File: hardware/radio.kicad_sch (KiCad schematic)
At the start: 44 parts, among them J101 Cortex_Debug, J102 JAE_DX07S016JA3, SW101 SW_Push, SW102 SW_Push, U101 TPS78433QWDRBRQ1, U102 ATSAMD51G, U103 E62, Y101 32k768

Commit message: Refresh
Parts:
- D101, D102: LCSC (none) -> C965555; Manufacturer (none) -> Worldsemi; Product (none) -> WS2812B-2020
- ESD101: Manufacturer (none) -> Semtech; Mouser (none) -> 947-RCLAMP0582N.TCT; Product (none) -> RCLAMP0582N.TCT
- J102: Manufacturer (none) -> JAE Electronics; Mouser (none) -> 656-DX07S016JA3R1500; Product (none) -> DX07S016JA3R1500
- TVS101: Manufacturer (none) -> Bourns; Mouser (none) -> 652-CG0603MLC-05LE; Product (none) -> CG0603MLC-05LE; Rating (none) -> 5V
- U101: Manufacturer (none) -> Texas Instruments; Mouser (none) -> 595-TPS78433QWDRBRQ1; Product (none) -> TPS78433QWDRBRQ1
- U102: Manufacturer (none) -> Microchip Technology; Mouser (none) -> 556-ATSAMD51G19AMU; Product (none) -> ATSAMD51G19A-MU
- renumbered C103 to C102, C104 to C103, C105 to C104, C106 to C105, C107 to C106, C108 to C107, C109 to C108, C110 to C109, C111 to C110, C303 to C111

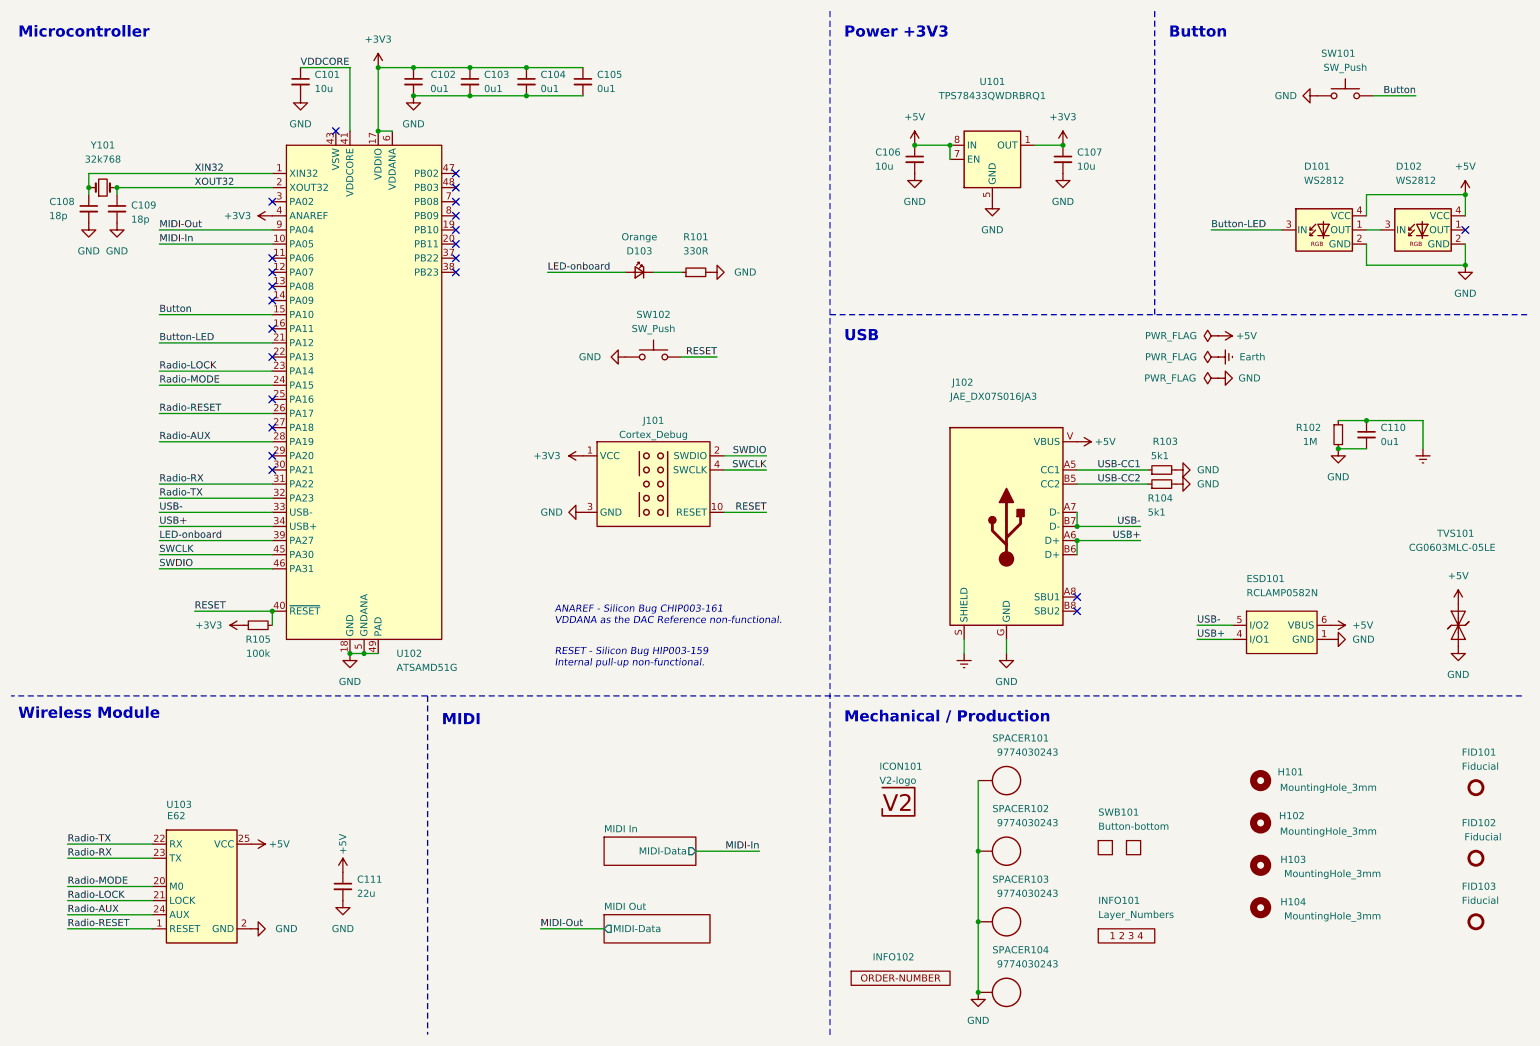
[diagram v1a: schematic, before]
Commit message: Replace Order_Number
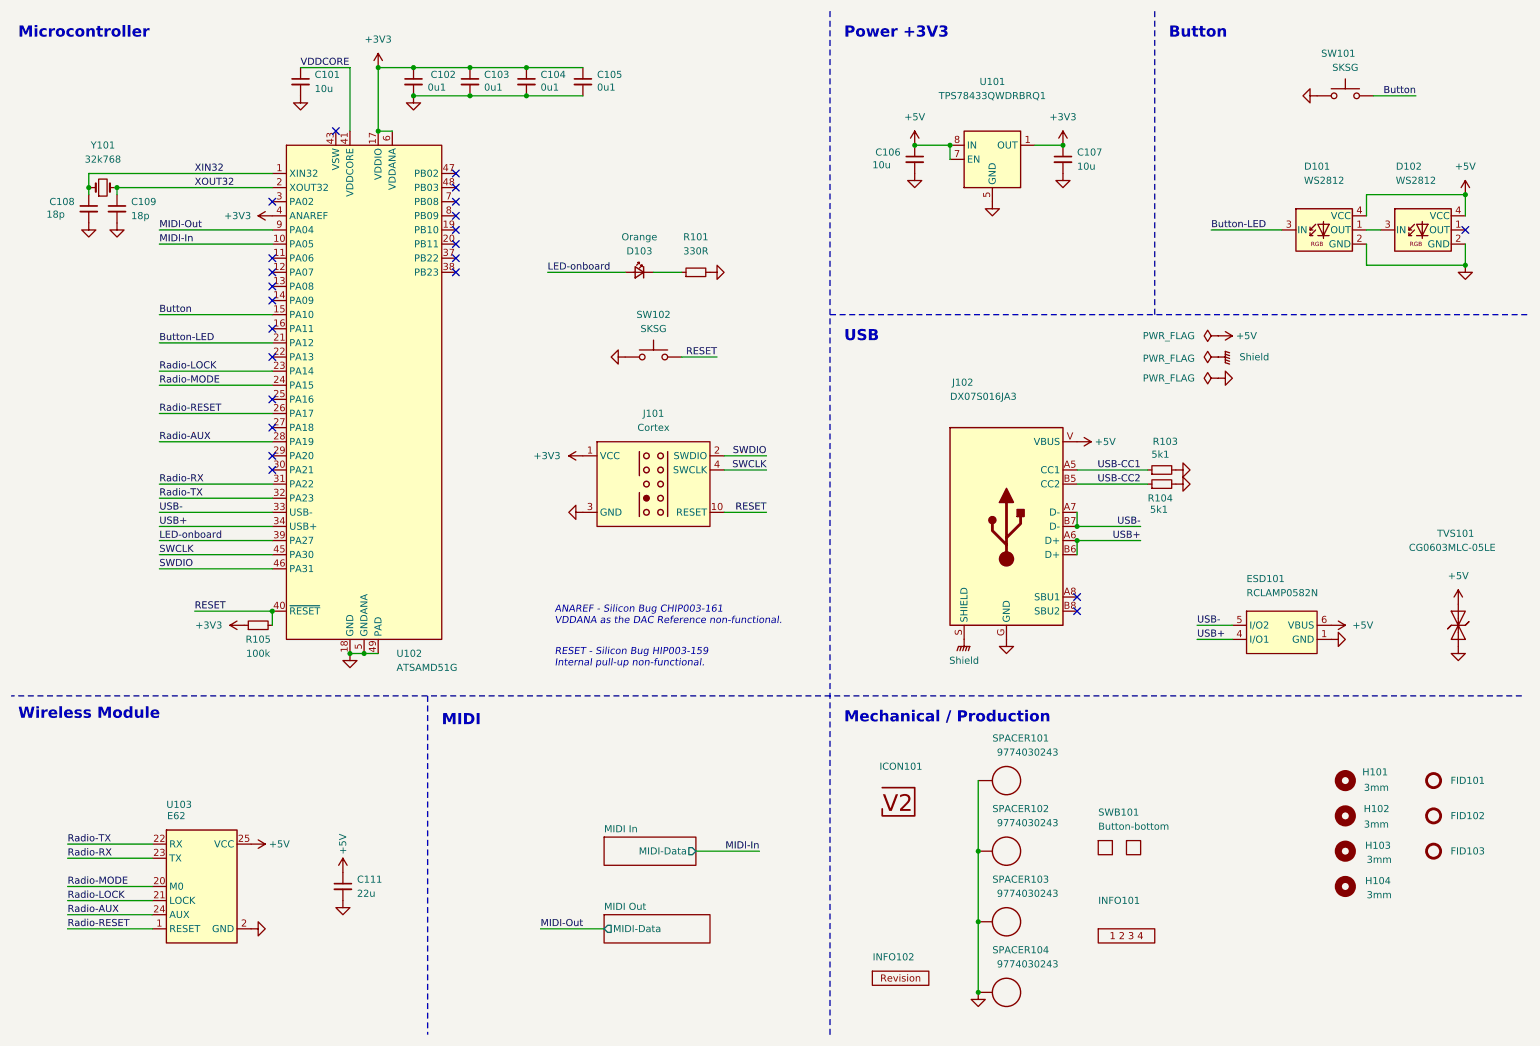
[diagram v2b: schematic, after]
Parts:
- removed C110: 0u1, Capacitor_SMD:C_0603_1608Metric, symbol Device:C_Small
- removed R102: 1M, Resistor_SMD:R_0603_1608Metric, symbol Device:R_Small
- C101: footprint Capacitor_SMD:C_0603_1608Metric -> V2_Capacitor_SMD:C_0603; symbol Device:C_Small -> V2_Device:C_0603_10u; Manufacturer (none) -> TDK; Mouser (none) -> 810-C1608X6S1A106M; Product (none) -> C1608X6S1A106M080AC; Rating (none) -> 10V
- C102, C103, C104, C105: footprint Capacitor_SMD:C_0603_1608Metric -> V2_Capacitor_SMD:C_0603; symbol Device:C_Small -> V2_Device:C_0603_0u1; Manufacturer (none) -> TDK; Mouser (none) -> 810-CGA3E2X7R1H104MA; Product (none) -> CGA3E2X7R1H104M080AA; Rating (none) -> 50V
- C106, C107: footprint Capacitor_SMD:C_0603_1608Metric -> V2_Capacitor_SMD:C_0805; symbol Device:C_Small -> V2_Device:C_0805_10u; Manufacturer (none) -> TDK; Mouser (none) -> 810-C2012X5R1E106K; Product (none) -> C2012X5R1E106K125AB; Rating (none) -> 25V
- C108, C109: footprint Capacitor_SMD:C_0603_1608Metric -> V2_Capacitor_SMD:C_0603; symbol Device:C_Small -> V2_Device:C_0603_18p; Manufacturer (none) -> YAGEO; Mouser (none) -> 603-CC603JRNPO9BN180; Product (none) -> CC0603JRNPO9BN180
- C111: footprint Capacitor_SMD:C_1210_3225Metric -> V2_Capacitor_SMD:C_1210; symbol Device:C_Small -> V2_Device:C_1210_22u; Manufacturer (none) -> TDK; Mouser (none) -> 810-CGA6P3X7R1E226M5; Product (none) -> CGA6P3X7R1E226M250AE; Rating (none) -> 25V
- D103: footprint LED_SMD:LED_0603_1608Metric -> V2_LED:LED_0603; symbol Device:LED_Small -> V2_Device:LED_0603_Orange; Manufacturer (none) -> ROHM Semiconductor; Mouser (none) -> 755-SML-D12D1WT86; Product (none) -> SML-D12D1WT86
- FID101, FID102, FID103: value Fiducial -> Fiducial_Paste
- H101, H102, H103, H104: value MountingHole_3mm -> 3mm
- INFO102: value ORDER-NUMBER -> ~; footprint V2_Production:Order_Number -> V2_Production:Revision; symbol V2_Production:Order_Number -> V2_Production:Revision
- J101: value Cortex_Debug -> Cortex; footprint V2_Cortex_Debug:Cortex_Debug_Pad -> V2_Connector_Debug:Cortex; symbol V2_Cortex_Debug:Cortex_Debug -> V2_Connector_Debug:Cortex
- J102: value JAE_DX07S016JA3 -> DX07S016JA3
- R101: footprint Resistor_SMD:R_0603_1608Metric -> V2_Resistor_SMD:R_0603; symbol Device:R_Small -> V2_Device:R_0603_330R; Manufacturer (none) -> Vishay; Mouser (none) -> 71-CRCW0603330RFKEAC; Product (none) -> CRCW0603330RFKEAC; Rating (none) -> 100mW
- R103, R104: footprint Resistor_SMD:R_0603_1608Metric -> V2_Resistor_SMD:R_0603; symbol Device:R_Small -> V2_Device:R_0603_5k1; Manufacturer (none) -> Vishay; Mouser (none) -> 71-CRCW06035K10FKEAC; Product (none) -> CRCW06035K10FKEAC; Rating (none) -> 100mW
- R105: footprint Resistor_SMD:R_0603_1608Metric -> V2_Resistor_SMD:R_0603; symbol Device:R_Small -> V2_Device:R_0603_100k; Manufacturer (none) -> Vishay; Mouser (none) -> 71-CRCW0603100KFKEAC; Product (none) -> CRCW0603100KFKEAC; Rating (none) -> 100mW
- SW101, SW102: value SW_Push -> SKSG; symbol Switch:SW_Push -> V2_Switch:SKSG; Manufacturer (none) -> Alps Alpine; Mouser (none) -> 688-SKSGACE010; Product (none) -> SKSGACE010
- TVS101: footprint Diode_SMD:D_0603_1608Metric -> V2_Diode_SMD:D_0603
- Y101: symbol Device:Crystal_Small -> V2_Device:Crystal_3.2x1.5_32k768; Manufacturer (none) -> ABRACON; Mouser (none) -> 815-ABS0716632.768KT; Product (none) -> ABS07-166-32.768KHZ-T
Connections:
- net Earth renamed Shield
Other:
- moved on the sheet: FID101, FID102, FID103, H101, H102, H103, H104

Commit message: Update Library
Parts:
- C101: symbol V2_Device:C_0603_10u -> V2_Capacitor:0603_10u
- C102, C103, C104, C105: symbol V2_Device:C_0603_0u1 -> V2_Capacitor:0603_0u1
- C106, C107: symbol V2_Device:C_0805_10u -> V2_Capacitor:0805_10u
- C108, C109: symbol V2_Device:C_0603_18p -> V2_Capacitor:0603_18p
- C111: value 22u -> 10u; symbol V2_Device:C_1210_22u -> V2_Capacitor:1210_22u
- D103: symbol V2_Device:LED_0603_Orange -> V2_LED:0603_Orange
- R101: symbol V2_Device:R_0603_330R -> V2_Resistor:0603_330R
- R103, R104: symbol V2_Device:R_0603_5k1 -> V2_Resistor:0603_5k1
- R105: symbol V2_Device:R_0603_100k -> V2_Resistor:0603_100k
- Y101: symbol V2_Device:Crystal_3.2x1.5_32k768 -> V2_Crystal:3.2x1.5_32k768

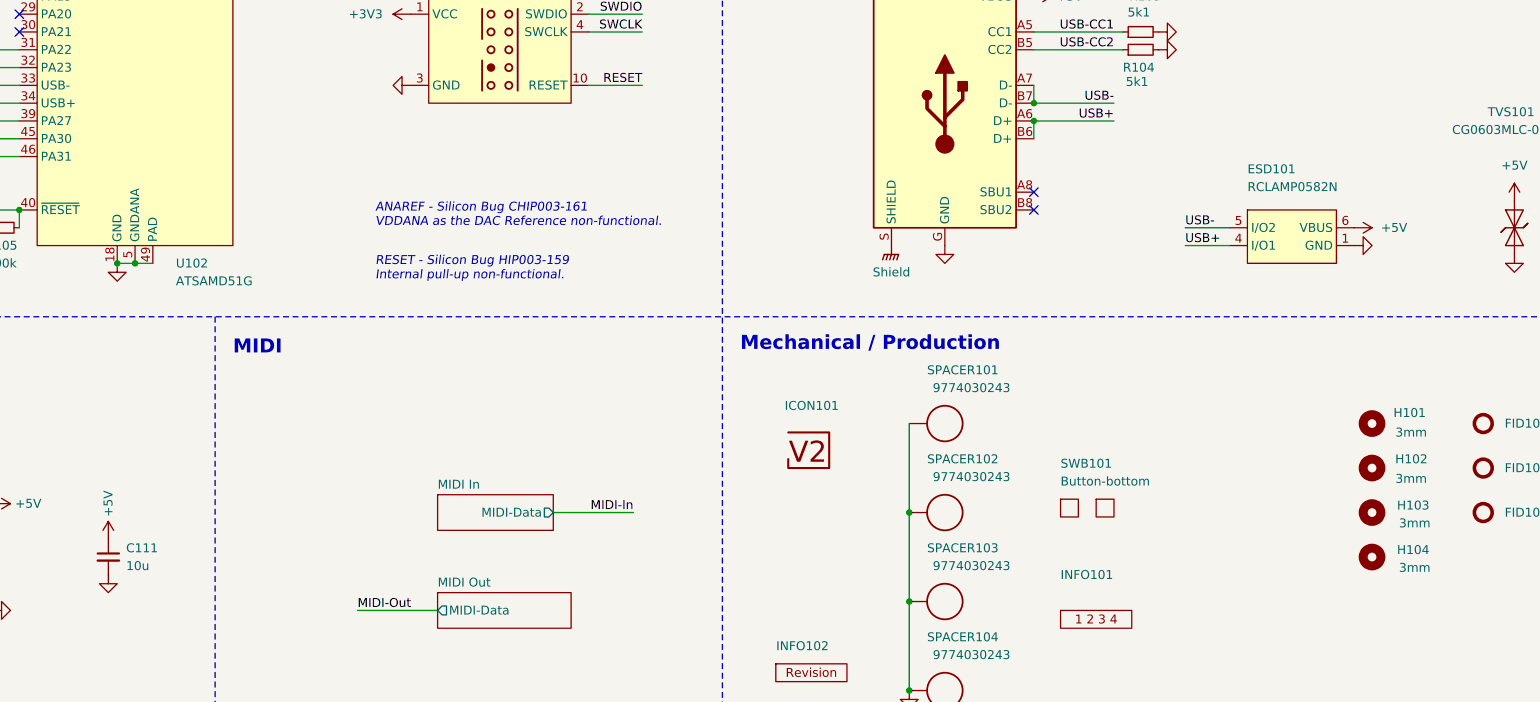
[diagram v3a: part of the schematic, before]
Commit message: Update ESD suppressor
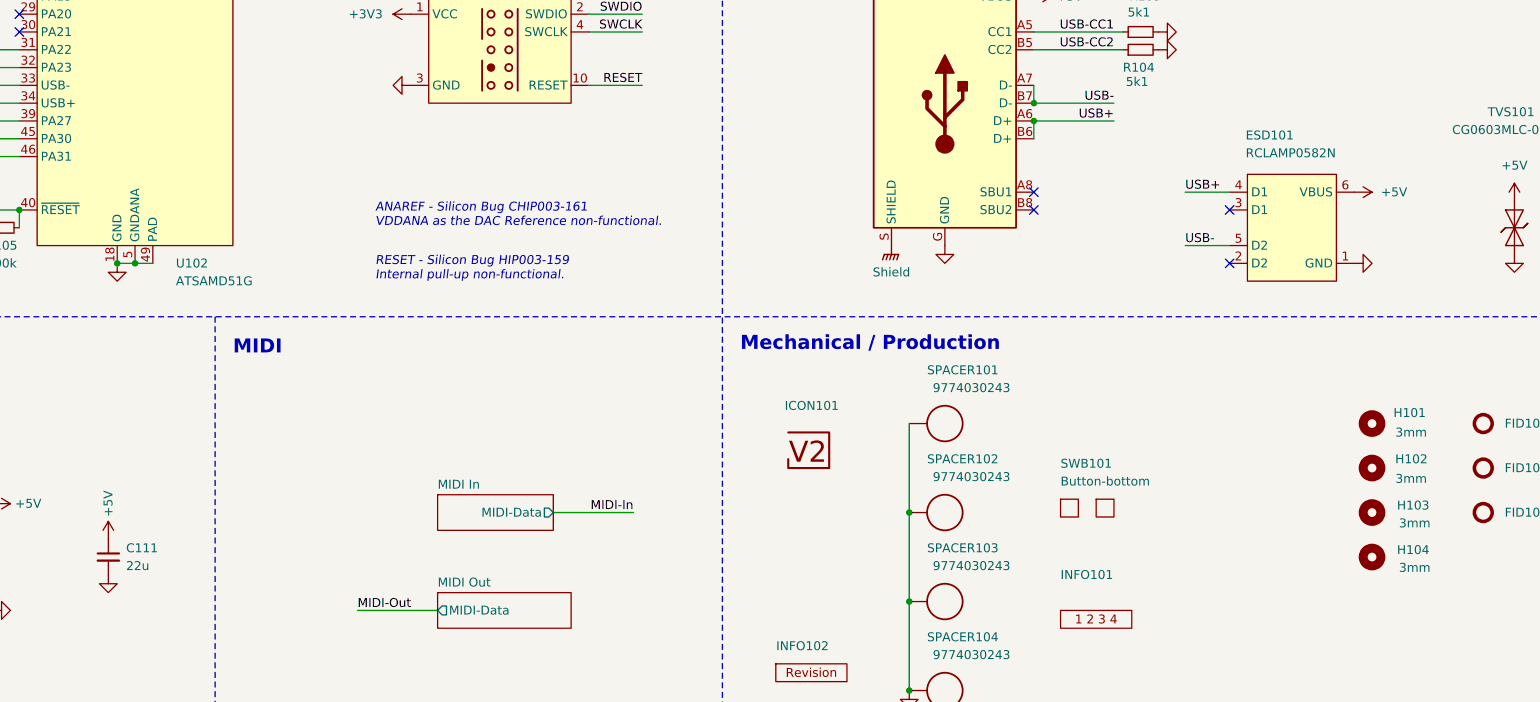
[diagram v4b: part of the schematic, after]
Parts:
- C108, C109: Manufacturer YAGEO -> TDK; Mouser 603-CC603JRNPO9BN180 -> 810-CGA3E2C0G1H180J; Product CC0603JRNPO9BN180 -> CGA3E2C0G1H180J080AA
- C111: value 10u -> 22u
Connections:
- no-connect marks 23 -> 25
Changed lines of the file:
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@@
 	(title_block
 		(title "V2 radio")
-		(date "2026-02-10")
+		(date "2026-03-14")
 		(rev "2026-02-10")
 		(company "Versio Duo")
@@
 	)
 	(no_connect
+		(at 232.41 120.65)
+	)
+	(no_connect
+		(at 232.41 128.27)
+	)
+	(no_connect
 		(at 71.12 34.29)
 	)
@@
 	(wire
 		(pts
-			(xy 226.06 123.19) (xy 232.41 123.19)
+			(xy 226.06 125.73) (xy 232.41 125.73)
 		)
 		(stroke
@@
 	(wire
 		(pts
+			(xy 226.06 118.11) (xy 232.41 118.11)
+		)
+		(stroke
+			(width 0)
+			(type default)
+		)
+	)
+	(wire
+		(pts
 			(xy 95.25 27.94) (xy 105.41 27.94)
 		)
@@
 	(wire
 		(pts
-			(xy 226.06 125.73) (xy 232.41 125.73)
-		)
-		(stroke
-			(width 0)
-			(type default)
-		)
-	)
-	(wire
-		(pts
 			(xy 109.22 59.69) (xy 123.19 59.69)
 		)
@@
 		)
 	)
-	(label "SWCLK"
-		(at 39.37 110.49 0)
+	(label "USB+"
+		(at 226.06 118.11 0)
 		(effects
 			(font
@@
 		)
 	)
-	(label "SWDIO"
-		(at 39.37 113.03 0)
+	(label "SWCLK"
+		(at 39.37 110.49 0)
 		(effects
 			(font
@@
 		)
 	)
-	(label "Button"
-		(at 39.37 67.31 0)
+	(label "SWDIO"
+		(at 39.37 113.03 0)
 		(effects
 			(font
@@
 		)
 	)
-	(label "USB+"
-		(at 226.06 125.73 0)
+	(label "Button"
+		(at 39.37 67.31 0)
 		(effects
 			(font
@@
 	)
 	(label "USB-"
-		(at 226.06 123.19 0)
+		(at 226.06 125.73 0)
 		(effects
 			(font
@@
 			)
 		)
-		(property "Description" "Unpolarized capacitor, small symbol"
+		(property "Description" ""
 			(at 115.57 38.1 0)
 			(effects
@@
 		(dnp no)
 		(property "Reference" "ESD101"
-			(at 234.95 115.57 0)
+			(at 234.696 110.744 0)
 			(effects
 				(font
@@
 		)
 		(property "Value" "RCLAMP0582N"
-			(at 234.95 118.11 0)
+			(at 234.696 113.284 0)
 			(effects
 				(font
@@
 			)
 		)
-		(property "Description" "Push button switch, generic, two pins"
+		(property "Description" "Push button"
 			(at 252.73 27.94 0)
 			(effects
@@
 	(symbol
 		(lib_id "V2_power:+5V")
-		(at 250.19 123.19 270)
+		(at 250.19 118.11 270)
 		(unit 1)
 		(exclude_from_sim no)
@@
 		(dnp no)
 		(property "Reference" "#PWR129"
-			(at 246.38 123.19 0)
+			(at 246.38 118.11 0)
 			(effects
 				(font
@@
 		)
 		(property "Value" "+5V"
-			(at 254 123.19 90)
+			(at 254 118.11 90)
 			(effects
 				(font
@@
 		)
 		(property "Footprint" ""
-			(at 250.19 123.19 0)
+			(at 250.19 118.11 0)
 			(effects
 				(font
@@
 		)
 		(property "Datasheet" ""
-			(at 250.19 123.19 0)
+			(at 250.19 118.11 0)
 			(effects
 				(font
@@
 		)
 		(property "Description" ""
-			(at 250.19 123.19 0)
+			(at 250.19 118.11 0)
 			(effects
 				(font
@@
 			)
 		)
-		(property "Description" "Light emitting diode, small symbol"
+		(property "Description" ""
 			(at 125.73 59.69 0)
 			(effects
@@
 			)
 		)
-		(property "Description" "Unpolarized capacitor, small symbol"
+		(property "Description" ""
 			(at 201.93 52.07 0)
 			(effects
@@
 			)
 		)
-		(property "Description" "Resistor, small symbol"
+		(property "Description" ""
 			(at 232.41 97.79 0)
 			(effects
@@
 			)
 		)
-		(property "Value" "10u"
+		(property "Value" "22u"
 			(at 74.93 171.45 0)
 			(effects
@@
 			)
 		)
-		(property "Description" "Unpolarized capacitor, small symbol"
+		(property "Description" ""
 			(at 72.39 182.88 0)
 			(effects
@@
 			)
 		)
-		(property "Description" "Unpolarized capacitor, small symbol"
+		(property "Description" ""
 			(at 175.26 52.07 0)
 			(effects
@@
 			)
 		)
-		(property "Description" "Two pin crystal, small symbol"
+		(property "Description" ""
 			(at 29.21 44.45 0)
 			(effects
@@
 			)
 		)
-		(property "Description" "Unpolarized capacitor, small symbol"
+		(property "Description" ""
 			(at 31.75 62.738 0)
 			(effects
@@
 			)
 		)
-		(property "Mouser" "603-CC603JRNPO9BN180"
+		(property "Mouser" "810-CGA3E2C0G1H180J"
 			(at 31.75 71.628 0)
 			(effects
@@
 			)
 		)
-		(property "Product" "CC0603JRNPO9BN180"
+		(property "Product" "CGA3E2C0G1H180J080AA"
 			(at 31.75 68.834 0)
 			(effects
@@
 			)
 		)
-		(property "Manufacturer" "YAGEO"
+		(property "Manufacturer" "TDK"
 			(at 31.75 66.04 0)
 			(effects
@@
 			)
 		)
-		(property "Description" "Unpolarized capacitor, small symbol"
+		(property "Description" ""
 			(at 64.77 40.64 0)
 			(effects
@@
 			)
 		)
-		(property "Description" "Unpolarized capacitor, small symbol"
+		(property "Description" ""
 			(at 26.67 62.738 0)
 			(effects
@@
 			)
 		)
-		(property "Mouser" "603-CC603JRNPO9BN180"
+		(property "Mouser" "810-CGA3E2C0G1H180J"
 			(at 26.67 71.628 0)
 			(effects
@@
 			)
 		)
-		(property "Product" "CC0603JRNPO9BN180"
+		(property "Product" "CGA3E2C0G1H180J080AA"
 			(at 26.67 68.834 0)
 			(effects
@@
 			)
 		)
-		(property "Manufacturer" "YAGEO"
+		(property "Manufacturer" "TDK"
 			(at 26.67 66.04 0)
 			(effects
@@
 			)
 		)
-		(property "Description" "Resistor, small symbol"
+		(property "Description" ""
 			(at 148.59 59.69 0)
 			(effects
@@
 	(symbol
 		(lib_id "V2_power:GND")
-		(at 250.19 125.73 90)
+		(at 250.19 128.27 90)
 		(unit 1)
 		(exclude_from_sim no)
@@
 		(dnp no)
 		(property "Reference" "#PWR130"
-			(at 256.54 125.73 0)
+			(at 256.54 128.27 0)
 			(effects
 				(font
@@
 		)
 		(property "Value" "GND"
-			(at 254 125.73 90)
+			(at 254 128.27 90)
 			(effects
 				(font
@@
 		)
 		(property "Footprint" ""
-			(at 250.19 125.73 0)
+			(at 250.19 128.27 0)
 			(effects
 				(font
@@
 		)
 		(property "Datasheet" ""
-			(at 250.19 125.73 0)
+			(at 250.19 128.27 0)
 			(effects
 				(font
@@
 		)
 		(property "Description" ""
-			(at 250.19 125.73 0)
+			(at 250.19 128.27 0)
 			(effects
 				(font
@@
 			)
 		)
-		(property "Description" "Unpolarized capacitor, small symbol"
+		(property "Description" ""
 			(at 105.41 38.1 0)
 			(effects
@@
 			)
 		)
-		(property "Description" "Unpolarized capacitor, small symbol"
+		(property "Description" ""
 			(at 85.09 38.1 0)
 			(effects
@@
 			)
 		)
-		(property "Description" "Push button switch, generic, two pins"
+		(property "Description" "Push button"
 			(at 128.27 74.93 0)
 			(effects
@@
 			)
 		)
-		(property "Description" "Unpolarized capacitor, small symbol"
+		(property "Description" ""
 			(at 95.25 38.1 0)
 			(effects
@@
 			)
 		)
-		(property "Description" "Resistor, small symbol"
+		(property "Description" ""
 			(at 232.41 95.25 0)
 			(effects
@@
 			)
 		)
-		(property "Description" "Resistor, small symbol"
+		(property "Description" ""
 			(at 69.85 123.19 0)
 			(effects

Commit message: Replace diode
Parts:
- INFO102: value ~ -> (none)
